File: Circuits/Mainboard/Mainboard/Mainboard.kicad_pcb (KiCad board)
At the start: 2 copper layers, 160 x 160 mm, 43 parts, among them IC1 LM74500QDDFRQ1, IC2 LM74500QDDFRQ1, IC3 WSEN-ISDS 6-Dof IMU, IC4 SX1280IMLTRT, IC5 SKY66122-11, IC6 TS2596CM533_RNG, J1 XT60PW-M, J2 XT60PW-M, J4 Conn_01x05_Pin, J5 B6B-PH-K-S, J6 B5P-VH_LF__SN_, Q1 PSMN6R7-40MLDX, Q2 PSMN6R7-40MLDX, U1 NUCLEOH723ZG

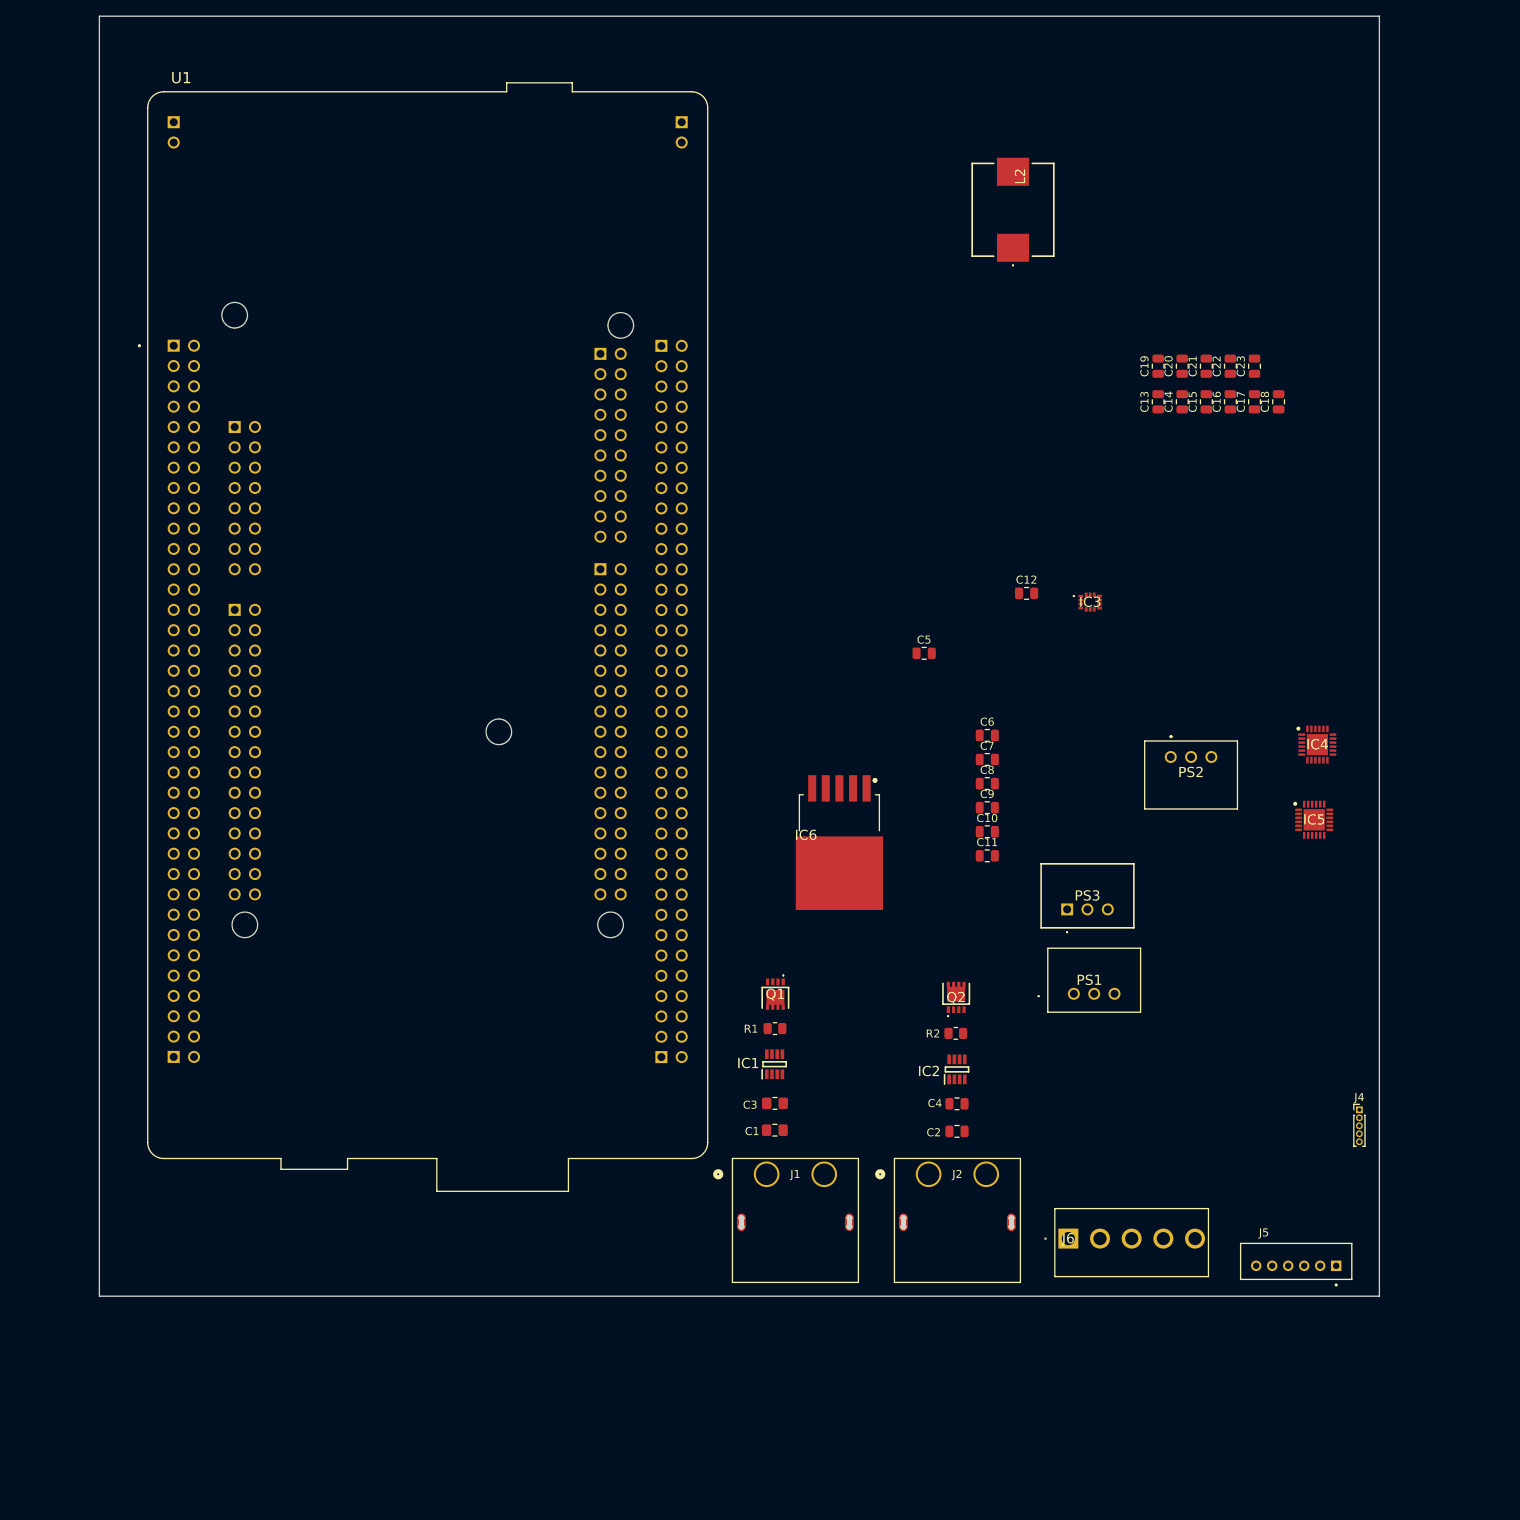
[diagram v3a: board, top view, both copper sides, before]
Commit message: Added components for mainboard
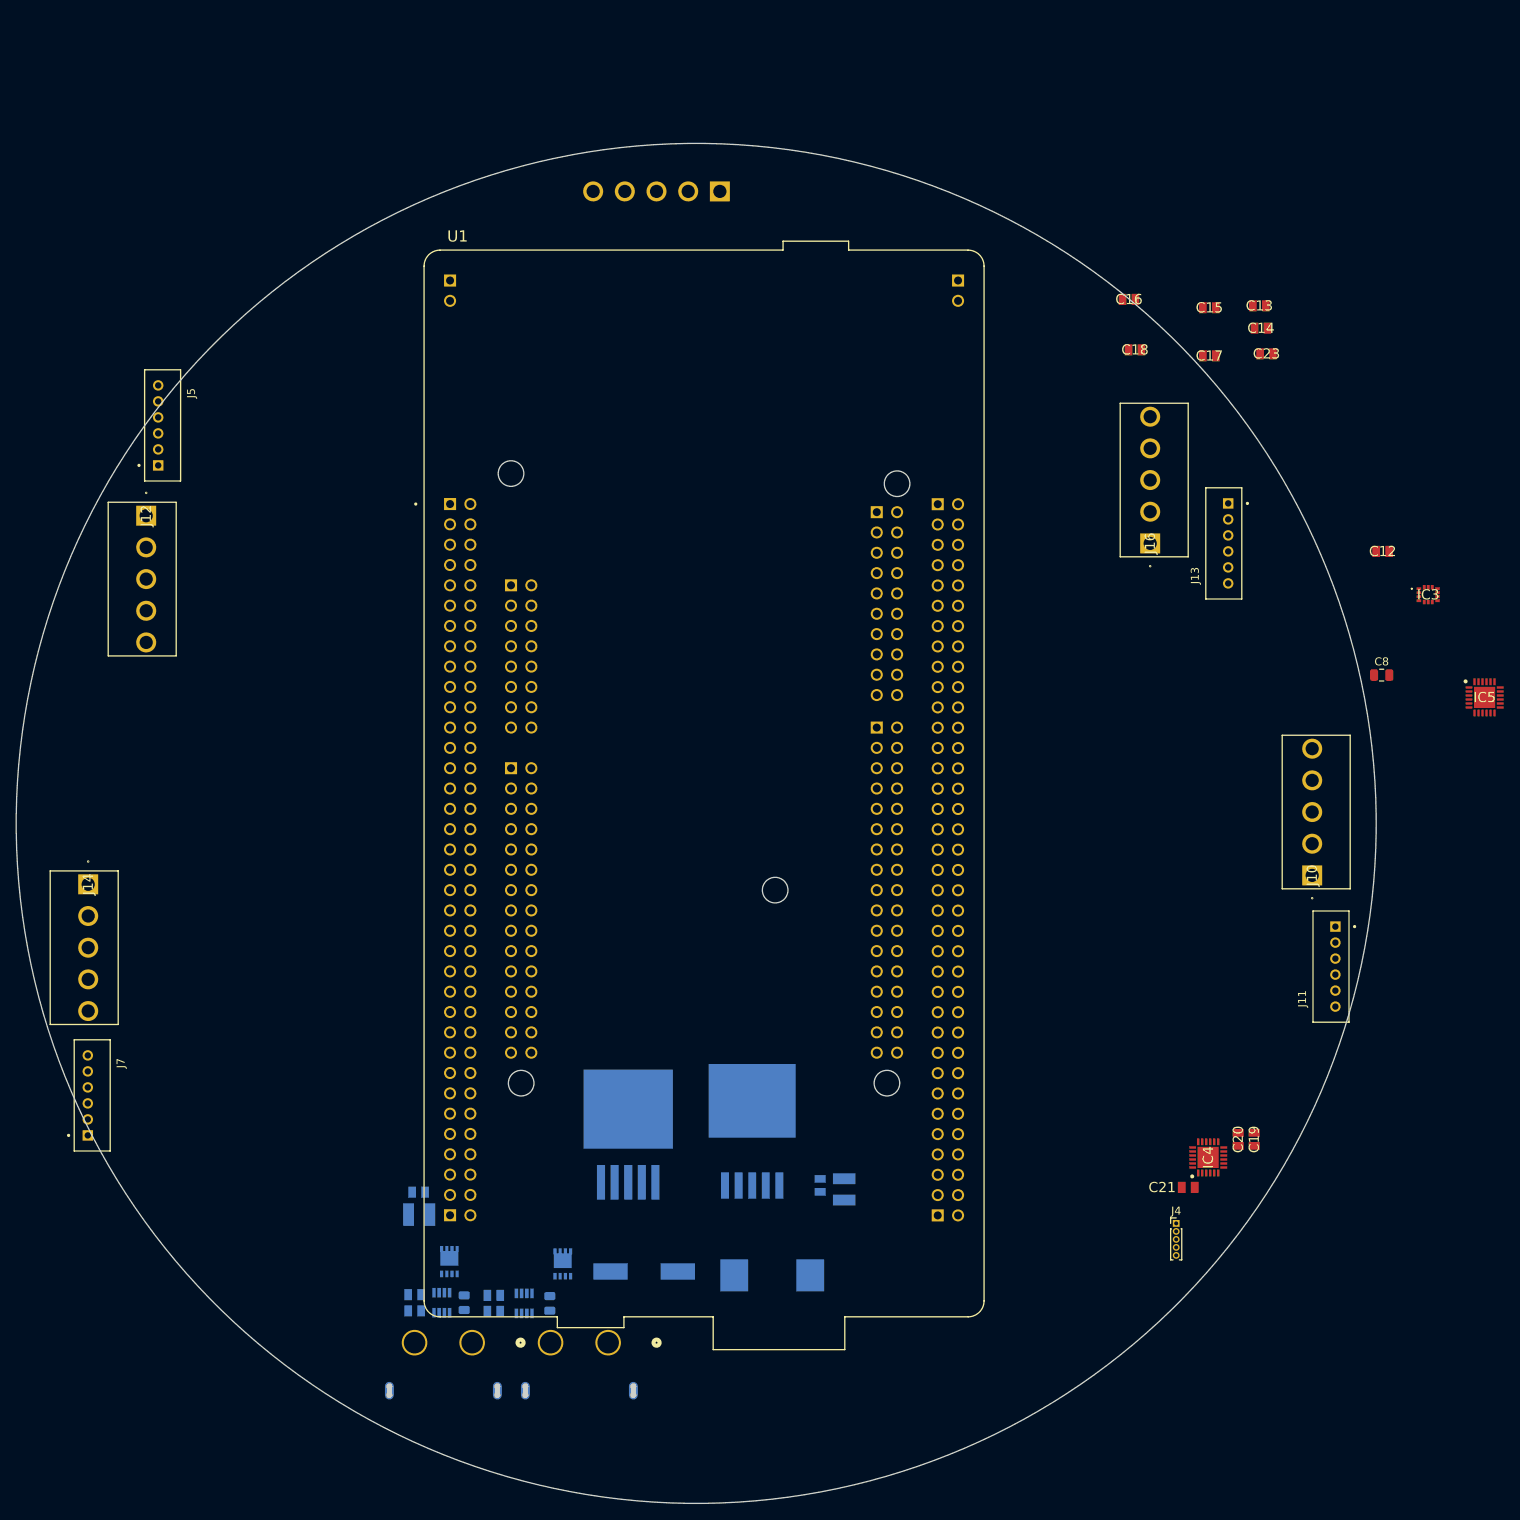
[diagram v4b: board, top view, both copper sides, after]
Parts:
- removed C11: 10uF, Capacitor_SMD:C_0805_2012Metric
- removed C22: 470uF, Capacitor_SMD:C_0805_2012Metric
- removed PS1: 3.3V Step down, FDSM 3.3V:173010335
- removed PS2: 5V Step down, FDSM 5V:173010542
- removed PS3: 12V Step down, FDSM 12V:173011235
- added IC7: LM2576-5.0WU-TR, LM2576-5.0WU-TR:5-PIN-TO-263_U_, B.Cu at (178.0, 161.4)
- added J10: B5P-VH_LF__SN_, B5P-VH-LF-SN:B5P-VH_LF__SN_, F.Cu at (263.5, 135.0)
- added J11: B6B-PH-K-S, B6B-PH-K-S:JST_B6B-PH-K-S, F.Cu at (265.9, 146.4)
- added J12: B5P-VH_LF__SN_, B5P-VH-LF-SN:B5P-VH_LF__SN_, F.Cu at (117.8, 90.0)
- added J13: B6B-PH-K-S, B6B-PH-K-S:JST_B6B-PH-K-S, F.Cu at (252.4, 93.5)
- added J14: B5P-VH_LF__SN_, B5P-VH-LF-SN:B5P-VH_LF__SN_, F.Cu at (110.5, 136.1)
- added J16: B5P-VH_LF__SN_, B5P-VH-LF-SN:B5P-VH_LF__SN_, F.Cu at (243.2, 93.5)
- added J7: B6B-PH-K-S, B6B-PH-K-S:JST_B6B-PH-K-S, F.Cu at (111.0, 162.5)
- C1, C3: footprint Capacitor_SMD:C_0805_2012Metric_Pad1.18x1.45mm_HandSolder -> 885012007063:CAPC2012X90N; moved to B.Cu
- C10, C9: footprint Capacitor_SMD:C_0805_2012Metric -> 885012209073:CAPC3225X280N; moved to B.Cu
- C12, C13, C14, C15, C16, C17, C18, C19, C20, C21, C23: footprint Capacitor_SMD:C_0805_2012Metric -> 885012007063:CAPC2012X90N
- C2, C4, C6, C7: footprint Capacitor_SMD:C_0805_2012Metric -> 885012007063:CAPC2012X90N; moved to B.Cu
- C5: footprint Capacitor_SMD:C_0805_2012Metric -> 865080657018:CAPAE1030X1050N; moved to B.Cu
- IC1, IC2, IC6, J1, J2, J6, L2, Q1, Q2, R1, R2: moved to B.Cu
- moved J5 176.1 mm to (119.8, 78.8), turned to -90 degrees
- moved J6 138.0 mm to (189.5, 49.5), turned to 180 degrees
- moved L2 136.6 mm to (196.0, 185.0), turned to 180 degrees
- moved C21 102.7 mm to (248.0, 174.0), turned to 180 degrees
- moved C19 97.4 mm to (256.2, 168.0)
- moved C20 96.9 mm to (254.2, 168.0)
- moved C7 89.3 mm to (151.8, 174.6), turned to 180 degrees
- moved C10 85.6 mm to (151.9, 177.4), turned to 180 degrees
- moved C5 84.8 mm to (180.0, 184.5), turned to 180 degrees
- moved C4 71.9 mm to (151.3, 187.4)
- moved Q2 71.4 mm to (155.7, 183.2), turned to 180 degrees
- moved C2 71.4 mm to (151.3, 189.4)
- moved IC2 70.7 mm to (154.7, 188.4), turned to -90 degrees
- moved R2 70.1 mm to (157.5, 188.4), turned to -90 degrees
- moved J2 60.8 mm to (158.5, 193.4), turned to 180 degrees
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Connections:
- C10 pad 1: /24V -> 24V
- C13 pad 1: /3.3V -> GND
- C13 pad 2: GND -> 3.3V
- C14 pad 1: /3.3V -> 3.3V
- C15 pad 1: /3.3V -> 3.3V
- C16 pad 1: /3.3V -> 3.3V
- C17 pad 1: /3.3V -> 3.3V
- C18 pad 1: /3.3V -> 3.3V
- C23 pad 1: /3.3V -> 3.3V
- C5 pad 1: /24V -> 24V
- C6 pad 1: /24V -> 24V
- C7 pad 1: /24V -> 24V
- C9 pad 1: /24V -> 24V
- IC4 pad 15: /3.3V -> 3.3V
- IC6 pad 1: /24V -> 24V
- IC6 pad 4: /3.3V -> 3.3V
- J4 pad 1: /3.3V -> 3.3V
- L2 pad 2: /3.3V -> 3.3V
- Q1 pad 10: /24V -> 24V
- Q1 pad 11: /24V -> 24V
- Q1 pad 5: /24V -> 24V
- Q1 pad 6: /24V -> 24V
- Q1 pad 7: /24V -> 24V
- Q1 pad 8: /24V -> 24V
- Q1 pad 9: /24V -> 24V
- Q2 pad 10: /24V -> 24V
- Q2 pad 11: /24V -> 24V
- Q2 pad 5: /24V -> 24V
- Q2 pad 6: /24V -> 24V
- Q2 pad 7: /24V -> 24V
- Q2 pad 8: /24V -> 24V
- Q2 pad 9: /24V -> 24V
- U1 pad CN8_7: /3.3V -> 3.3V
- U1 pad CN8_8: /3.3V -> 3.3V
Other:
- board size 160 x 160 mm -> 170 x 170 mm

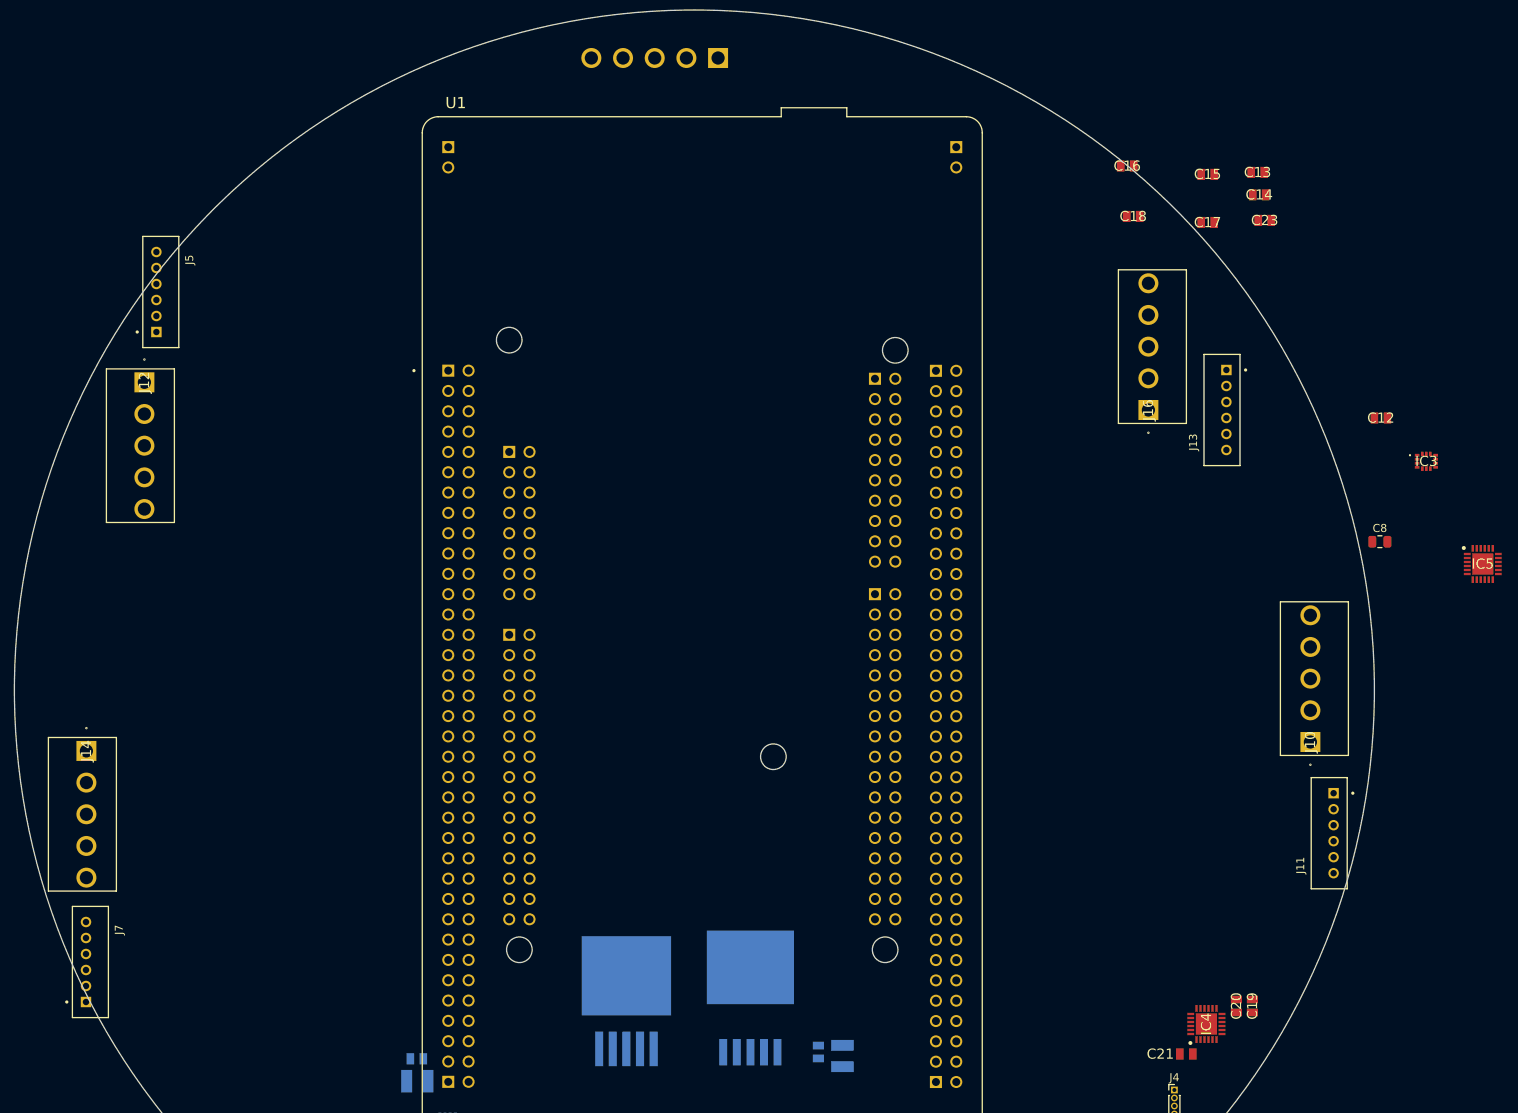
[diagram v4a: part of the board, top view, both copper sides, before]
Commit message: Added components for mainboard
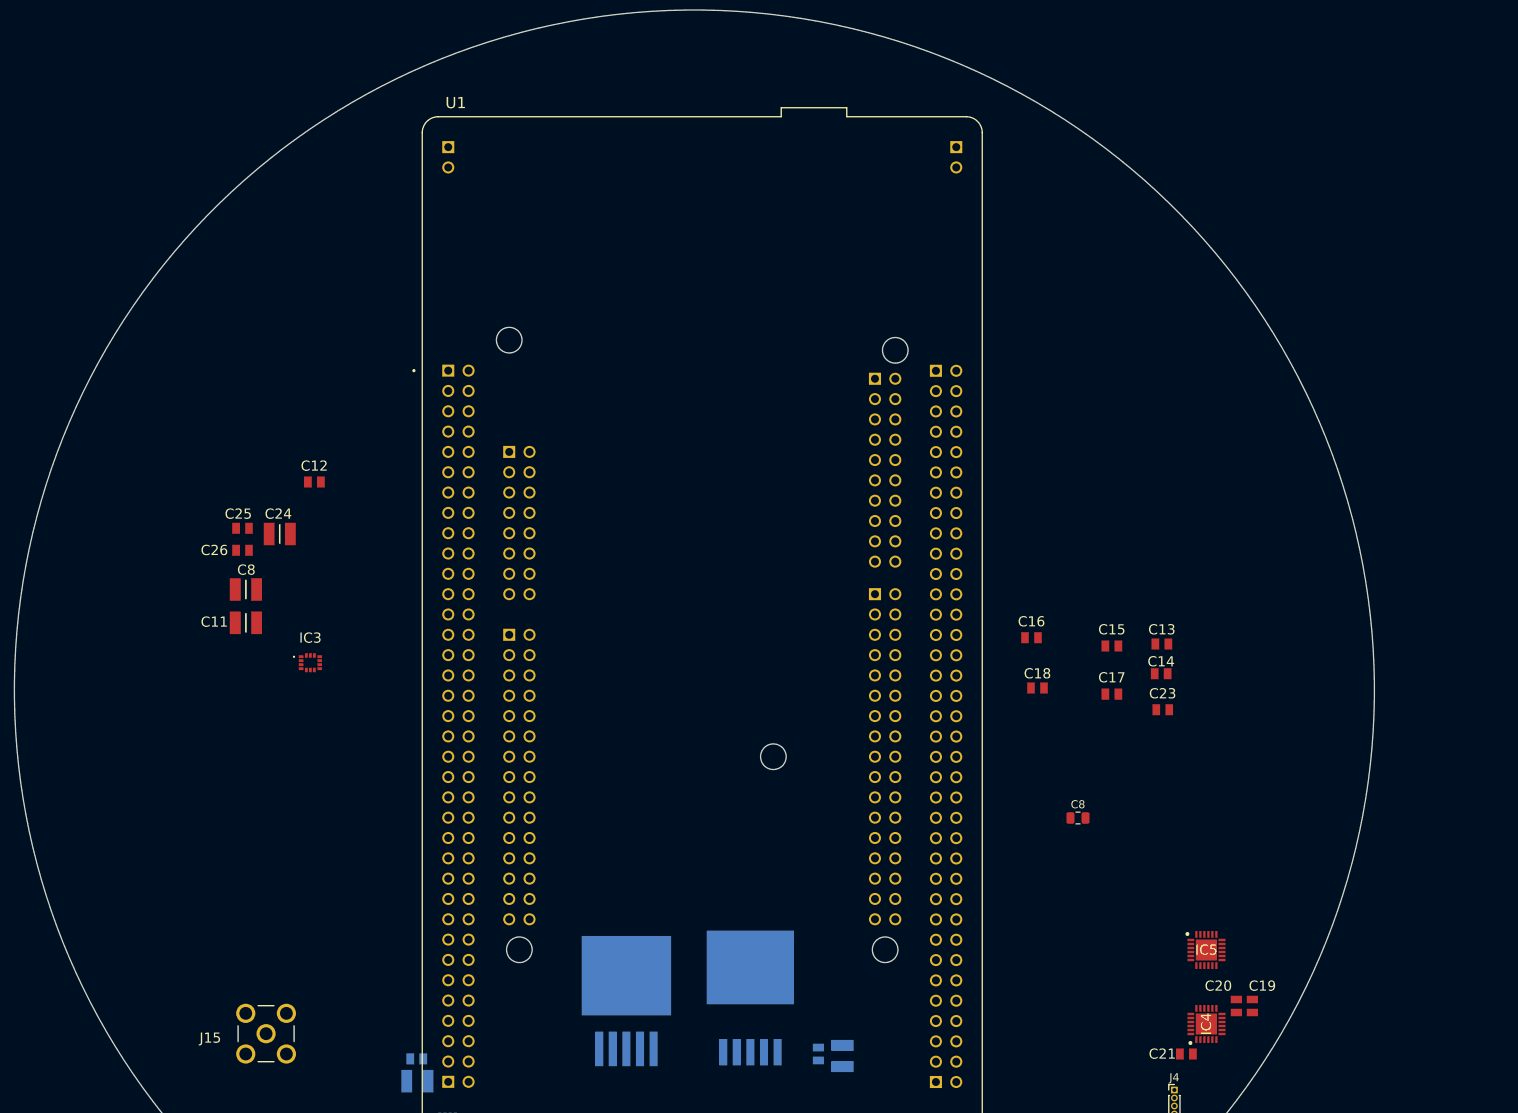
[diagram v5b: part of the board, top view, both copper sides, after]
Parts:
- removed J10, J12, J14, J16, J6: B5P-VH_LF__SN_, B5P-VH-LF-SN:B5P-VH_LF__SN_
- removed J11, J13, J5, J7: B6B-PH-K-S, B6B-PH-K-S:JST_B6B-PH-K-S
- added C11: 10uF, 885012209073:CAPC3225X280N, F.Cu at (130.4, 120.1)
- added C24: 10uF, 885012209073:CAPC3225X280N, F.Cu at (134.7, 109.0)
- added C25: 0.1uF, 885012007063:CAPC2012X90N, F.Cu at (130.0, 108.3)
- added C26: 0.1uF, 885012007063:CAPC2012X90N, F.Cu at (130.0, 111.0)
- added C8: 10uF, 885012209073:CAPC3225X280N, F.Cu at (130.4, 115.9)
- added J15: SMA-J-P-H-RA-TH1, SMA-J-P-H-RA-TH1:SMAJPHRATH1, F.Cu at (133.0, 171.5)
- IC3: value WSEN-ISDS 6-Dof IMU -> 2536030320001
- moved IC3 141.8 mm to (138.5, 125.1)
- moved C12 133.5 mm to (139.0, 102.5)
- moved C23 62.5 mm to (245.0, 131.0)
- moved C14 61.1 mm to (244.8, 126.5)
- moved C17 60.2 mm to (238.7, 129.0)
- moved C13 60.2 mm to (244.9, 122.8)
- moved C15 60.2 mm to (238.7, 123.0)
- moved C16 60.2 mm to (228.6, 122.0)
- moved C18 60.2 mm to (229.4, 128.3)
- moved IC5 59.3 mm to (250.5, 161.0)
- moved C8 51.2 mm to (234.4, 144.5)
- moved C6 0.25 mm to (202.0, 174.0)
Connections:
- IC3 pad 1: unconnected-(IC3-SAO-Pad1) -> WSENS_SAO
- IC3 pad 12: unconnected-(IC3-CS-Pad12) -> WSENS_CS
- IC3 pad 13: unconnected-(IC3-SCL-Pad13) -> WSENS_SCL
- IC3 pad 14: unconnected-(IC3-SDA-Pad14) -> WSENS_SDA
- IC3 pad 5: unconnected-(IC3-VDD_IO-Pad5) -> VDD_IO
- IC3 pad 6: unconnected-(IC3-GND_1-Pad6) -> GND
- IC3 pad 7: unconnected-(IC3-GND_2-Pad7) -> GND
- IC3 pad 8: unconnected-(IC3-VDD-Pad8) -> 3.3V
- U1 pad CN11_21: unconnected-(U1A-PB7-PadCN11_21) -> /BNO055_SDA
- U1 pad CN11_32: unconnected-(U1A-PA4-PadCN11_32) -> WSENS_CS
- U1 pad CN11_45: unconnected-(U1A-PD7-PadCN11_45) -> WSENS_SDA
- U1 pad CN11_51: unconnected-(U1A-PF1-PadCN11_51) -> /VL53L1_SCL
- U1 pad CN11_53: unconnected-(U1A-PF0-PadCN11_53) -> /VL53L1_SDA
- U1 pad CN12_1: unconnected-(U1B-PC9-PadCN12_1) -> /VL6180_SDA
- U1 pad CN12_11: unconnected-(U1B-PA5-PadCN12_11) -> WSENS_SCL
- U1 pad CN12_13: unconnected-(U1B-PA6-PadCN12_13) -> WSENS_SAO
- U1 pad CN12_23: unconnected-(U1B-PA8-PadCN12_23) -> /VL6180_SCL
- U1 pad CN12_3: unconnected-(U1B-PB8-PadCN12_3) -> /BNO055_SCL
